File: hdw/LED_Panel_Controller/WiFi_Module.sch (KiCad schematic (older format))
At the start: 37 parts

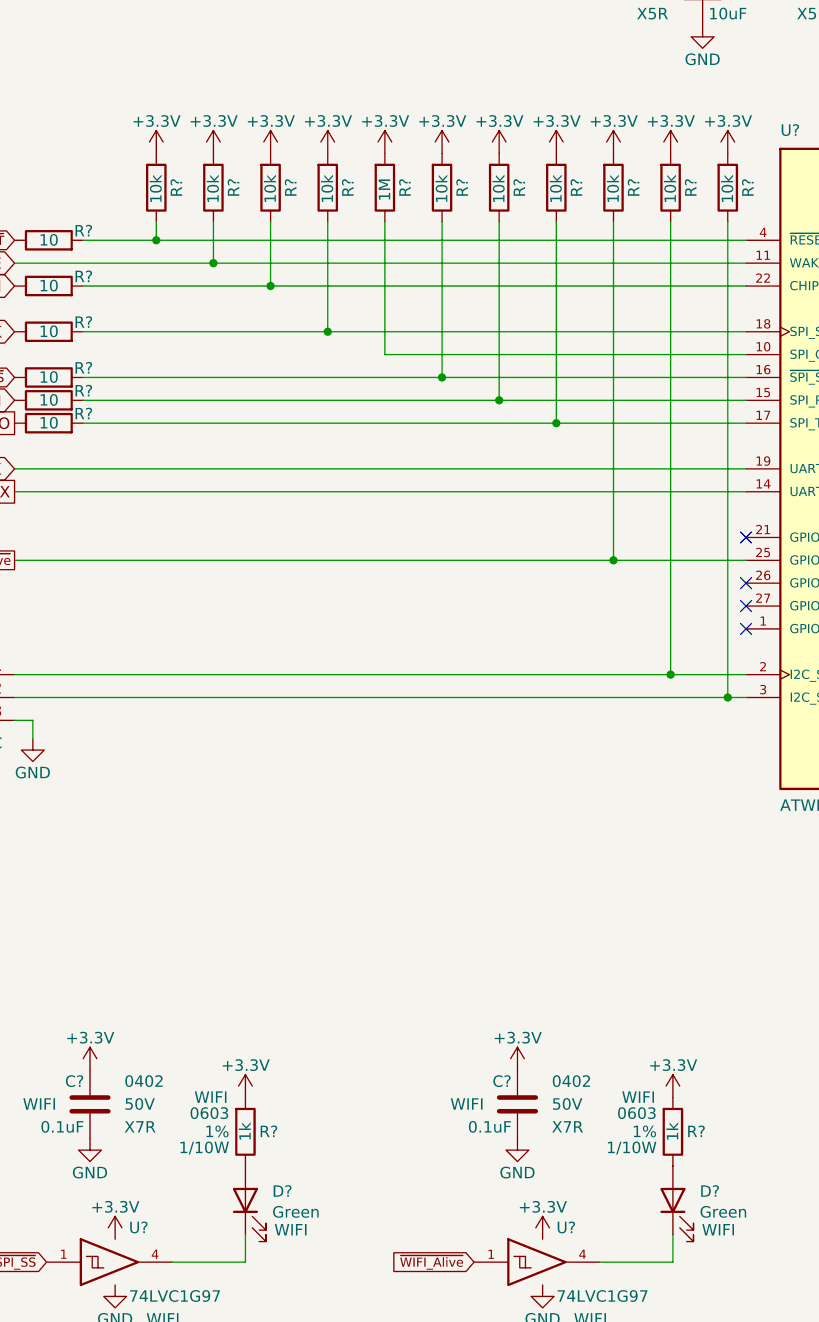
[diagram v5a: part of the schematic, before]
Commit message: added digikey pns, footprints, bom scrubbed
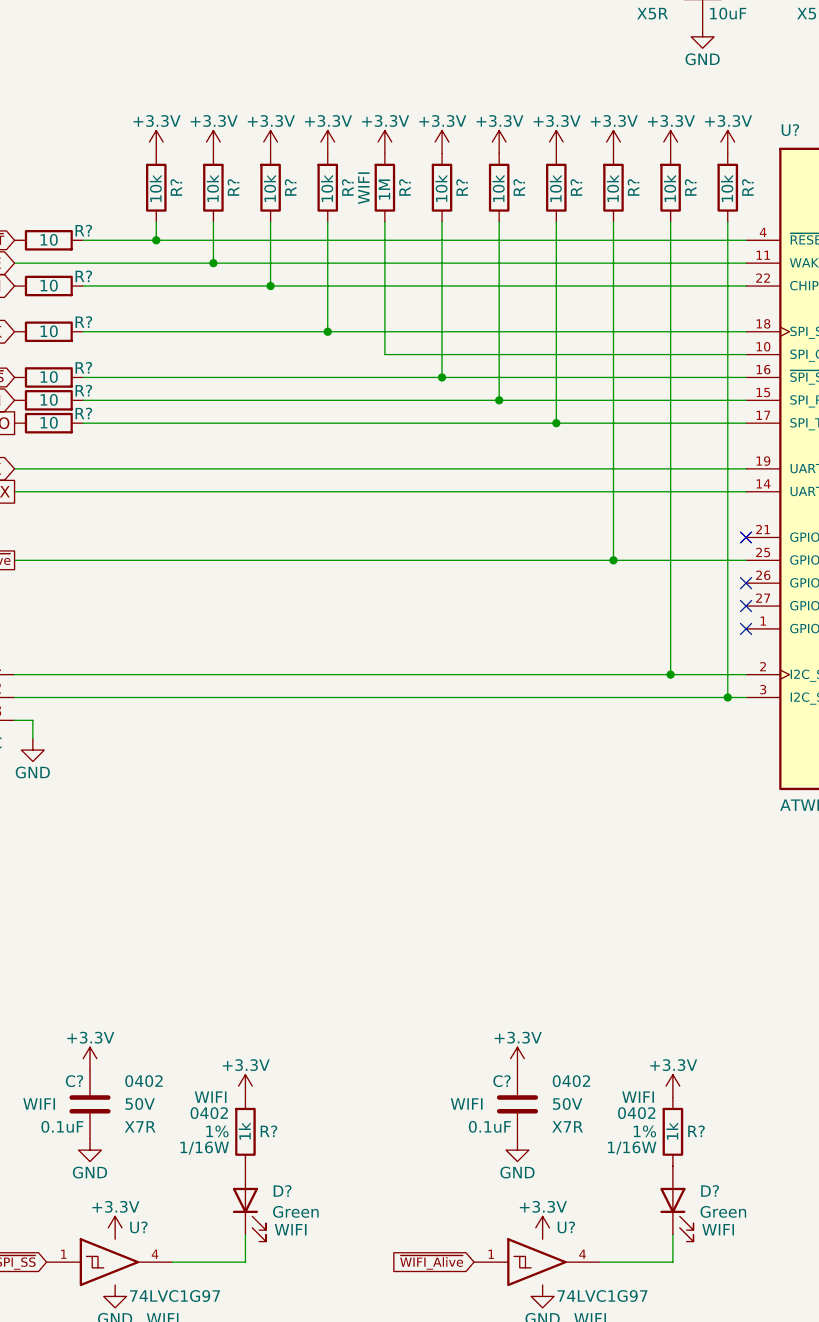
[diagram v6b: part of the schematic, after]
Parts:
- C?: footprint (none) -> Capacitors_SMD:C_0402; Digi-Key PN (none) -> 399-3066-1-ND
- C? (x5): Digi-Key PN 490-13211-1-ND -> 1276-1451-1-ND
- D? (x2): footprint LEDs:LED_0603 -> LEDs:LED_0402; Digi-Key PN 754-1121-1-ND -> 1497-1219-1-ND
- J?: footprint (none) -> Connector_PinHeader_2.54mm:PinHeader_1x03_P2.54mm_Vertical; Configuration (none) -> DNP
- R? (x12): Digi-Key PN (none) -> RMCF0402FT10K0CT-ND
- R? (x7): Digi-Key PN (none) -> RMCF0402FT10R0CT-ND
- R?: Configuration (none) -> WIFI; Digi-Key PN (none) -> RMCF0402FT1M00CT-ND
- R? (x2): footprint Resistors_SMD:R_0603 -> Resistors_SMD:R_0402; Digi-Key PN 311-1.00KHRCT-ND -> RMCF0402FT1K00CT-ND; Wattage 1/10W -> 1/16W; display_footprint 0603 -> 0402
- TP?: value TP_Pad -> TP
- U? (x2): Digi-Key PN (none) -> 1727-1772-1-ND
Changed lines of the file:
@@
 F 0 "C?" H 7355 3630 50  0000 L CNN
 F 1 "10nF" H 7355 3430 50  0000 L CNN
-F 2 "" H 7368 3380 50  0001 C CNN
+F 2 "Capacitors_SMD:C_0402" H 7368 3380 50  0001 C CNN
 F 3 "" H 7355 3630 50  0001 C CNN
 F 4 "0402" H 7180 3630 50  0000 R CNN "display_footprint"
@@
 F 6 "X7R" H 7180 3430 50  0000 R CNN "Dielectric"
 F 7 "WIFI" H 7180 3710 50  0000 R CNN "Configuration"
+F 8 "399-3066-1-ND" H 7330 3530 50  0001 C CNN "Digi-Key PN"
 	1    7330 3530
 	1    0    0    -1
@@
 F 5 "6.3V" H 7930 3530 50  0000 R CNN "Voltage"
 F 6 "X5R" H 7930 3430 50  0000 R CNN "Dielectric"
-F 7 "490-13211-1-ND" H 8080 3530 50  0001 C CNN "Digi-Key PN"
+F 7 "1276-1451-1-ND" H 8080 3530 50  0001 C CNN "Digi-Key PN"
 F 8 "WIFI" H 7930 3710 50  0000 R CNN "Configuration"
 	1    8080 3530
@@
 AR Path="/5F582E44/5FF27EFA" Ref="TP?"  Part="1"
 F 0 "TP?" H 8080 3370 50  0000 C CNN
-F 1 "TP_Pad" H 8080 3370 50  0001 C CNN
+F 1 "TP" H 8080 3370 50  0001 C CNN
 F 2 "Custom Footprints Library:Test_Point" H 8080 3220 60  0001 C CNN
 F 3 "" H 8080 3220 60  0000 C CNN
@@
 F 5 "1%" H 5520 2440 50  0001 L CNN "Tolerance"
 F 6 "1/16W" H 5520 2340 50  0001 L CNN "Wattage"
+F 7 "RMCF0402FT10K0CT-ND" H 5420 2470 50  0001 C CNN "Digi-Key PN"
 	1    5420 2470
 	-1   0    0    -1
@@
 F 5 "1%" H 5270 2440 50  0001 L CNN "Tolerance"
 F 6 "1/16W" H 5270 2340 50  0001 L CNN "Wattage"
+F 7 "RMCF0402FT10K0CT-ND" H 5170 2470 50  0001 C CNN "Digi-Key PN"
 	1    5170 2470
 	-1   0    0    -1
@@
 F 5 "1%" H 4520 2440 50  0001 L CNN "Tolerance"
 F 6 "1/16W" H 4520 2340 50  0001 L CNN "Wattage"
+F 7 "RMCF0402FT10K0CT-ND" H 4420 2470 50  0001 C CNN "Digi-Key PN"
 	1    4420 2470
 	-1   0    0    -1
@@
 F 5 "1%" H 5020 2440 50  0001 L CNN "Tolerance"
 F 6 "1/16W" H 5020 2340 50  0001 L CNN "Wattage"
+F 7 "RMCF0402FT10K0CT-ND" H 4920 2470 50  0001 C CNN "Digi-Key PN"
 	1    4920 2470
 	-1   0    0    -1
@@
 F 5 "1%" H 4770 2440 50  0001 L CNN "Tolerance"
 F 6 "1/16W" H 4770 2340 50  0001 L CNN "Wattage"
+F 7 "RMCF0402FT10K0CT-ND" H 4670 2470 50  0001 C CNN "Digi-Key PN"
 	1    4670 2470
 	-1   0    0    -1
@@
 F 5 "1%" H 3270 2440 50  0001 L CNN "Tolerance"
 F 6 "1/16W" H 3270 2340 50  0001 L CNN "Wattage"
+F 7 "RMCF0402FT10K0CT-ND" H 3170 2470 50  0001 C CNN "Digi-Key PN"
 	1    3170 2470
 	-1   0    0    -1
@@
 F 5 "1%" V 2650 3100 50  0001 C CNN "Tolerance"
 F 6 "1/16W" V 2750 3100 50  0001 C CNN "Wattage"
+F 7 "RMCF0402FT10R0CT-ND" H 2450 3100 50  0001 C CNN "Digi-Key PN"
 	1    2450 3100
 	0    1    1    0
@@
 F 5 "1%" V 2650 3300 50  0001 C CNN "Tolerance"
 F 6 "1/16W" V 2750 3300 50  0001 C CNN "Wattage"
+F 7 "RMCF0402FT10R0CT-ND" H 2450 3300 50  0001 C CNN "Digi-Key PN"
 	1    2450 3300
 	0    1    1    0
@@
 F 5 "1%" V 2650 3400 50  0001 C CNN "Tolerance"
 F 6 "1/16W" V 2750 3400 50  0001 C CNN "Wattage"
+F 7 "RMCF0402FT10R0CT-ND" H 2450 3400 50  0001 C CNN "Digi-Key PN"
 	1    2450 3400
 	0    1    1    0
@@
 F 5 "1%" V 2650 3500 50  0001 C CNN "Tolerance"
 F 6 "1/16W" V 2750 3500 50  0001 C CNN "Wattage"
+F 7 "RMCF0402FT10R0CT-ND" H 2450 3500 50  0001 C CNN "Digi-Key PN"
 	1    2450 3500
 	0    1    1    0
@@
 F 5 "1%" V 2650 2700 50  0001 C CNN "Tolerance"
 F 6 "1/16W" V 2750 2700 50  0001 C CNN "Wattage"
+F 7 "RMCF0402FT10R0CT-ND" H 2450 2700 50  0001 C CNN "Digi-Key PN"
 	1    2450 2700
 	0    1    1    0
@@
 F 5 "1%" V 9390 2700 50  0001 C CNN "Tolerance"
 F 6 "1/16W" V 9490 2700 50  0001 C CNN "Wattage"
+F 7 "RMCF0402FT10R0CT-ND" H 9190 2700 50  0001 C CNN "Digi-Key PN"
 	1    9190 2700
 	0    -1   1    0
@@
 F 5 "1%" V 2650 2900 50  0001 C CNN "Tolerance"
 F 6 "1/16W" V 2750 2900 50  0001 C CNN "Wattage"
+F 7 "RMCF0402FT10R0CT-ND" H 2450 2900 50  0001 C CNN "Digi-Key PN"
 	1    2450 2900
 	0    1    1    0
@@
 F 0 "J?" H 2100 4900 50  0000 C CNN
 F 1 "WIFI_I2C" H 2100 4500 50  0000 C CNN
-F 2 "" H 2100 4700 50  0001 C CNN
+F 2 "Connector_PinHeader_2.54mm:PinHeader_1x03_P2.54mm_Vertical" H 2100 4700 50  0001 C CNN
 F 3 "~" H 2100 4700 50  0001 C CNN
+F 4 "DNP" H 2100 4700 50  0001 C CNN "Configuration"
 	1    2100 4700
 	-1   0    0    -1
@@
 F 5 "6.3V" H 5160 1610 50  0000 R CNN "Voltage"
 F 6 "X5R" H 5160 1510 50  0000 R CNN "Dielectric"
-F 7 "490-13211-1-ND" H 5310 1610 50  0001 C CNN "Digi-Key PN"
+F 7 "1276-1451-1-ND" H 5310 1610 50  0001 C CNN "Digi-Key PN"
 F 8 "WIFI" H 5150 1780 50  0000 R CNN "Configuration"
 	1    5310 1610
@@
 F 5 "6.3V" H 5860 1610 50  0000 R CNN "Voltage"
 F 6 "X5R" H 5860 1510 50  0000 R CNN "Dielectric"
-F 7 "490-13211-1-ND" H 6010 1610 50  0001 C CNN "Digi-Key PN"
+F 7 "1276-1451-1-ND" H 6010 1610 50  0001 C CNN "Digi-Key PN"
 F 8 "WIFI" H 5850 1780 50  0000 R CNN "Configuration"
 	1    6010 1610
@@
 F 5 "6.3V" H 6560 1610 50  0000 R CNN "Voltage"
 F 6 "X5R" H 6560 1510 50  0000 R CNN "Dielectric"
-F 7 "490-13211-1-ND" H 6710 1610 50  0001 C CNN "Digi-Key PN"
+F 7 "1276-1451-1-ND" H 6710 1610 50  0001 C CNN "Digi-Key PN"
 F 8 "WIFI" H 6550 1780 50  0000 R CNN "Configuration"
 	1    6710 1610
@@
 F 5 "6.3V" H 7260 1610 50  0000 R CNN "Voltage"
 F 6 "X5R" H 7260 1510 50  0000 R CNN "Dielectric"
-F 7 "490-13211-1-ND" H 7410 1610 50  0001 C CNN "Digi-Key PN"
+F 7 "1276-1451-1-ND" H 7410 1610 50  0001 C CNN "Digi-Key PN"
 F 8 "WIFI" H 7250 1780 50  0000 R CNN "Configuration"
 	1    7410 1610
@@
 F 6 "1/16W" H 8780 2800 50  0000 L CNN "Wattage"
 F 7 "DNP" H 8870 3080 50  0000 C CNN "Configuration"
+F 8 "RMCF0402FT10K0CT-ND" H 8680 2930 50  0001 C CNN "Digi-Key PN"
 	1    8680 2930
 	-1   0    0    -1
@@
 F 0 "D?" V 3349 6783 50  0000 R CNN
 F 1 "Green" V 3258 6783 50  0000 R CNN
-F 2 "LEDs:LED_0603" H 3310 6900 50  0001 C CNN
+F 2 "LEDs:LED_0402" H 3310 6900 50  0001 C CNN
 F 3 "~" H 3310 6900 50  0001 C CNN
-F 4 "754-1121-1-ND" H -1850 580 50  0001 C CNN "Digi-Key PN"
+F 4 "1497-1219-1-ND" H -1850 580 50  0001 C CNN "Digi-Key PN"
 F 5 "WIFI" V 3180 6700 50  0000 C CNN "Configuration"
 	1    3310 6900
@@
 F 0 "R?" H 3250 6600 50  0000 R CNN
 F 1 "1k" V 3310 6600 50  0000 C CNN
-F 2 "Resistors_SMD:R_0603" H 3310 6600 50  0001 C CNN
+F 2 "Resistors_SMD:R_0402" H 3310 6600 50  0001 C CNN
 F 3 "" H 3310 6600 50  0001 C CNN
-F 4 "0603" H 3380 6680 50  0000 L CNN "display_footprint"
+F 4 "0402" H 3380 6680 50  0000 L CNN "display_footprint"
 F 5 "1%" H 3380 6600 50  0000 L CNN "Tolerance"
-F 6 "1/10W" H 3380 6530 50  0000 L CNN "Wattage"
-F 7 "311-1.00KHRCT-ND" H 3610 7000 60  0001 C CNN "Digi-Key PN"
+F 6 "1/16W" H 3380 6530 50  0000 L CNN "Wattage"
+F 7 "RMCF0402FT1K00CT-ND" H 3610 7000 60  0001 C CNN "Digi-Key PN"
 F 8 "WIFI" H 3460 6750 50  0000 C CNN "Configuration"
 	1    3310 6600
@@
 F 5 "1%" H 3020 2440 50  0001 L CNN "Tolerance"
 F 6 "1/16W" H 3020 2340 50  0001 L CNN "Wattage"
+F 7 "RMCF0402FT10K0CT-ND" H 2920 2470 50  0001 C CNN "Digi-Key PN"
 	1    2920 2470
 	-1   0    0    -1
@@
 F 3 "http://www.ti.com/lit/ds/symlink/sn74lvc1g97.pdf" H 2790 7170 50  0001 C CNN
 F 4 "WIFI" H 2950 6920 50  0000 C CNN "Configuration"
+F 5 "1727-1772-1-ND" H 2740 7170 50  0001 C CNN "Digi-Key PN"
 	1    2740 7170
 	1    0    0    -1
@@
 F 0 "D?" V 5219 6783 50  0000 R CNN
 F 1 "Green" V 5128 6783 50  0000 R CNN
-F 2 "LEDs:LED_0603" H 5180 6900 50  0001 C CNN
+F 2 "LEDs:LED_0402" H 5180 6900 50  0001 C CNN
 F 3 "~" H 5180 6900 50  0001 C CNN
-F 4 "754-1121-1-ND" H 20  580 50  0001 C CNN "Digi-Key PN"
+F 4 "1497-1219-1-ND" H 20  580 50  0001 C CNN "Digi-Key PN"
 F 5 "WIFI" V 5050 6700 50  0000 C CNN "Configuration"
 	1    5180 6900
@@
 F 0 "R?" H 5120 6600 50  0000 R CNN
 F 1 "1k" V 5180 6600 50  0000 C CNN
-F 2 "Resistors_SMD:R_0603" H 5180 6600 50  0001 C CNN
+F 2 "Resistors_SMD:R_0402" H 5180 6600 50  0001 C CNN
 F 3 "" H 5180 6600 50  0001 C CNN
-F 4 "0603" H 5250 6680 50  0000 L CNN "display_footprint"
+F 4 "0402" H 5250 6680 50  0000 L CNN "display_footprint"
 F 5 "1%" H 5250 6600 50  0000 L CNN "Tolerance"
-F 6 "1/10W" H 5250 6530 50  0000 L CNN "Wattage"
-F 7 "311-1.00KHRCT-ND" H 5480 7000 60  0001 C CNN "Digi-Key PN"
+F 6 "1/16W" H 5250 6530 50  0000 L CNN "Wattage"
+F 7 "RMCF0402FT1K00CT-ND" H 5480 7000 60  0001 C CNN "Digi-Key PN"
 F 8 "WIFI" H 5330 6750 50  0000 C CNN "Configuration"
 	1    5180 6600
@@
 F 5 "1%" H 8780 2440 50  0000 L CNN "Tolerance"
 F 6 "1/16W" H 8780 2340 50  0000 L CNN "Wattage"
-F 7 "" H 8980 2870 60  0001 C CNN "Digi-Key PN"
+F 7 "RMCF0402FT10K0CT-ND" H 8980 2870 60  0001 C CNN "Digi-Key PN"
 	1    8680 2470
 	-1   0    0    -1
@@
 F 3 "http://www.ti.com/lit/ds/symlink/sn74lvc1g97.pdf" H 4660 7170 50  0001 C CNN
 F 4 "WIFI" H 4820 6920 50  0000 C CNN "Configuration"
+F 5 "1727-1772-1-ND" H 4610 7170 50  0001 C CNN "Digi-Key PN"
 	1    4610 7170
 	1    0    0    -1
@@
 F 5 "1%" H 3520 2440 50  0001 L CNN "Tolerance"
 F 6 "1/16W" H 3520 2340 50  0001 L CNN "Wattage"
+F 7 "RMCF0402FT10K0CT-ND" H 3420 2470 50  0001 C CNN "Digi-Key PN"
 	1    3420 2470
 	-1   0    0    -1
@@
 F 5 "1%" H 3770 2440 50  0001 L CNN "Tolerance"
 F 6 "1/16W" H 3770 2340 50  0001 L CNN "Wattage"
+F 7 "RMCF0402FT10K0CT-ND" H 3670 2470 50  0001 C CNN "Digi-Key PN"
 	1    3670 2470
 	-1   0    0    -1
@@
 F 5 "1%" H 4270 2440 50  0001 L CNN "Tolerance"
 F 6 "1/16W" H 4270 2340 50  0001 L CNN "Wattage"
+F 7 "RMCF0402FT10K0CT-ND" H 4170 2470 50  0001 C CNN "Digi-Key PN"
 	1    4170 2470
 	-1   0    0    -1
@@
 F 5 "1%" H 4020 2440 50  0001 L CNN "Tolerance"
 F 6 "1/16W" H 4020 2340 50  0001 L CNN "Wattage"
+F 7 "RMCF0402FT1M00CT-ND" H 3920 2470 50  0001 C CNN "Digi-Key PN"
+F 8 "WIFI" V 4010 2470 50  0000 C CNN "Configuration"
 	1    3920 2470
 	-1   0    0    -1

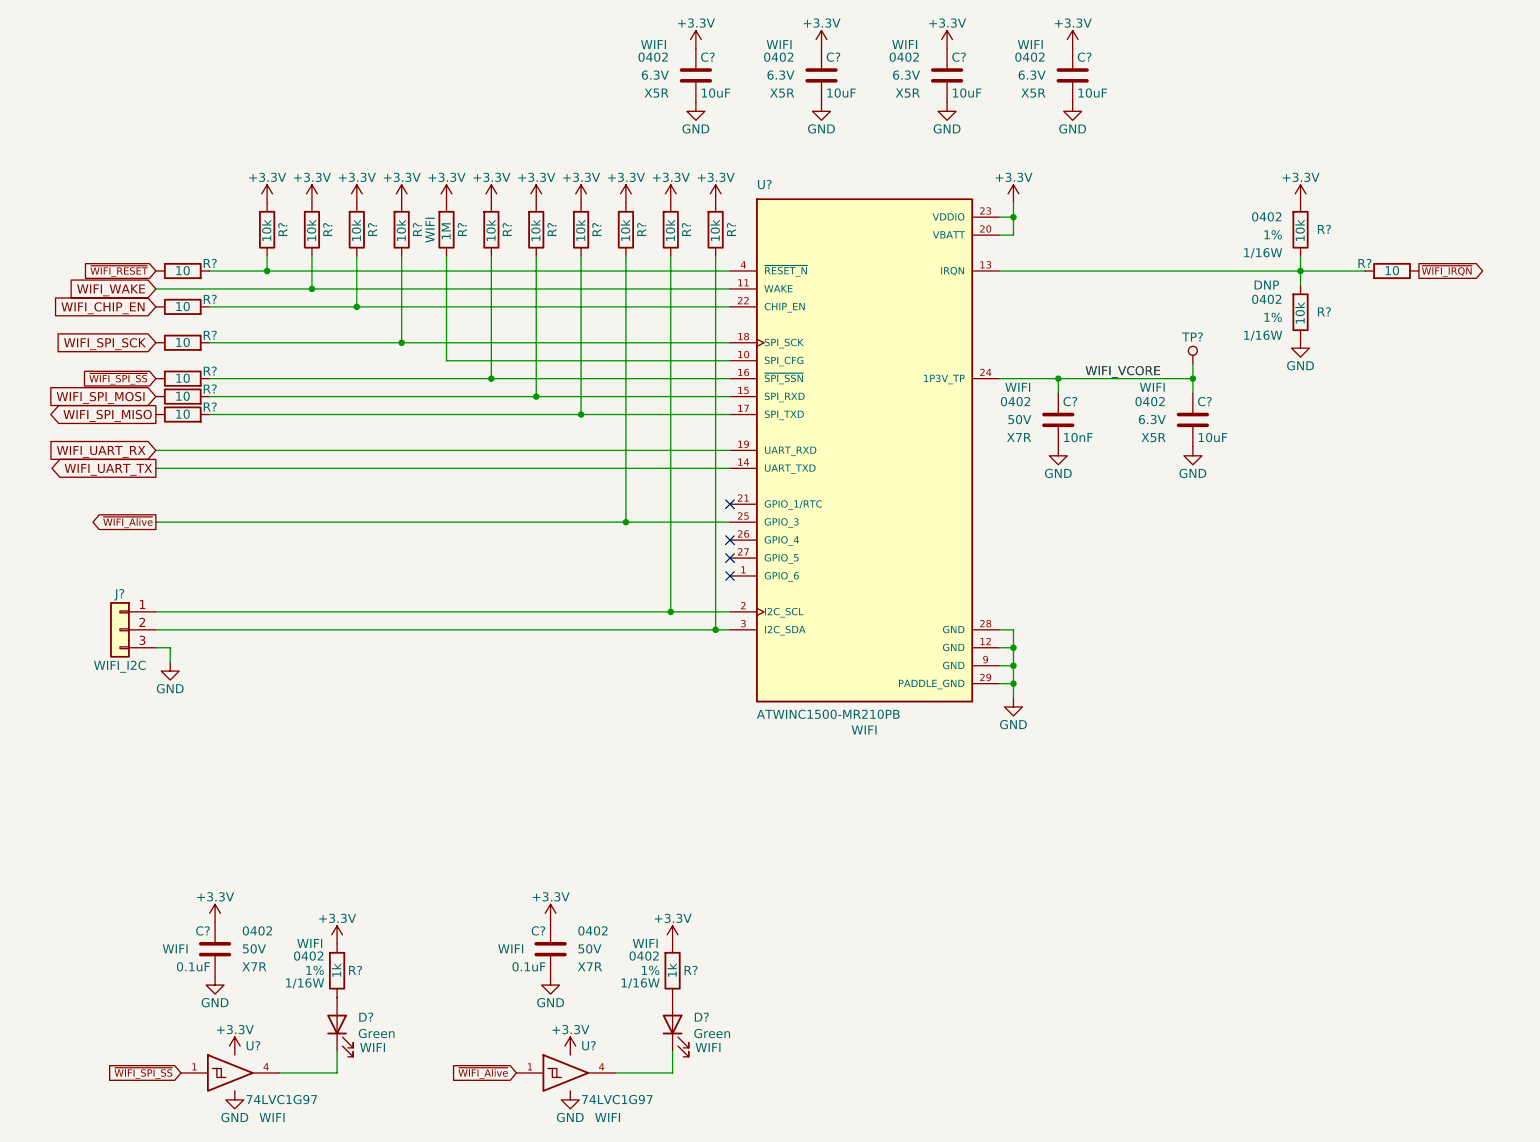
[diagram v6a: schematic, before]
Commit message: assigned I2C addresses
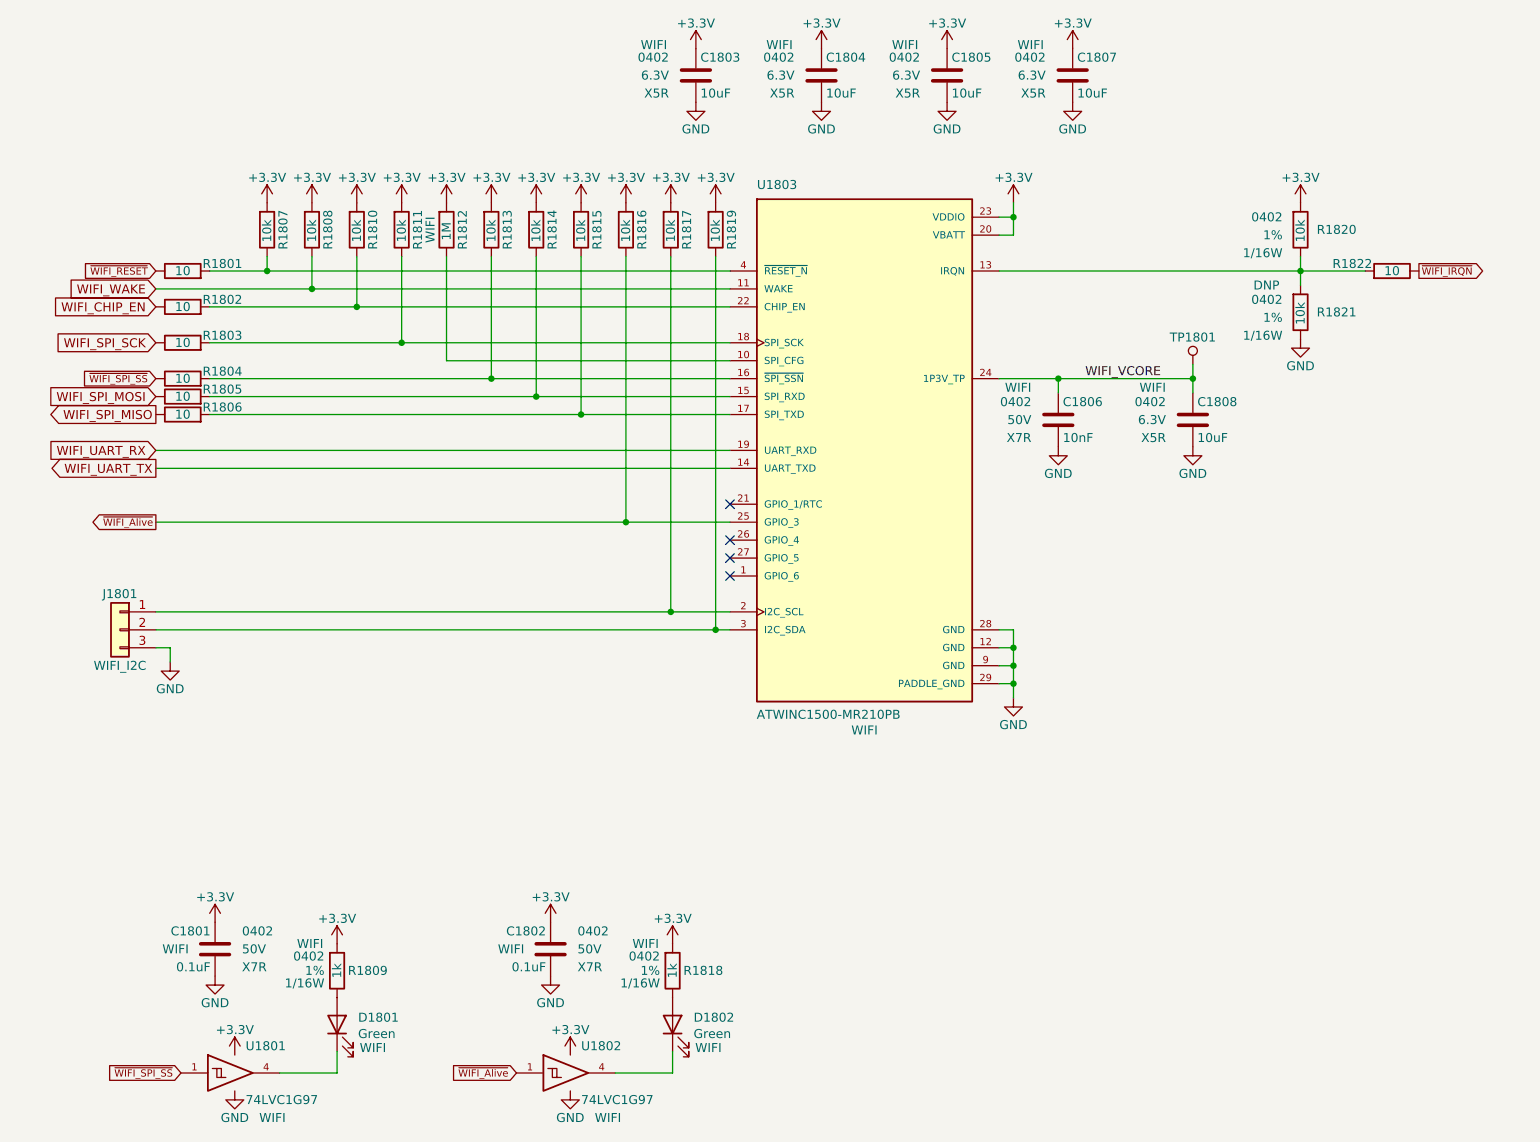
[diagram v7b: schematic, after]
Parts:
- gave numbers to parts that had none: 37
